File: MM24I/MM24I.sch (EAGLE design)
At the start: 7 parts

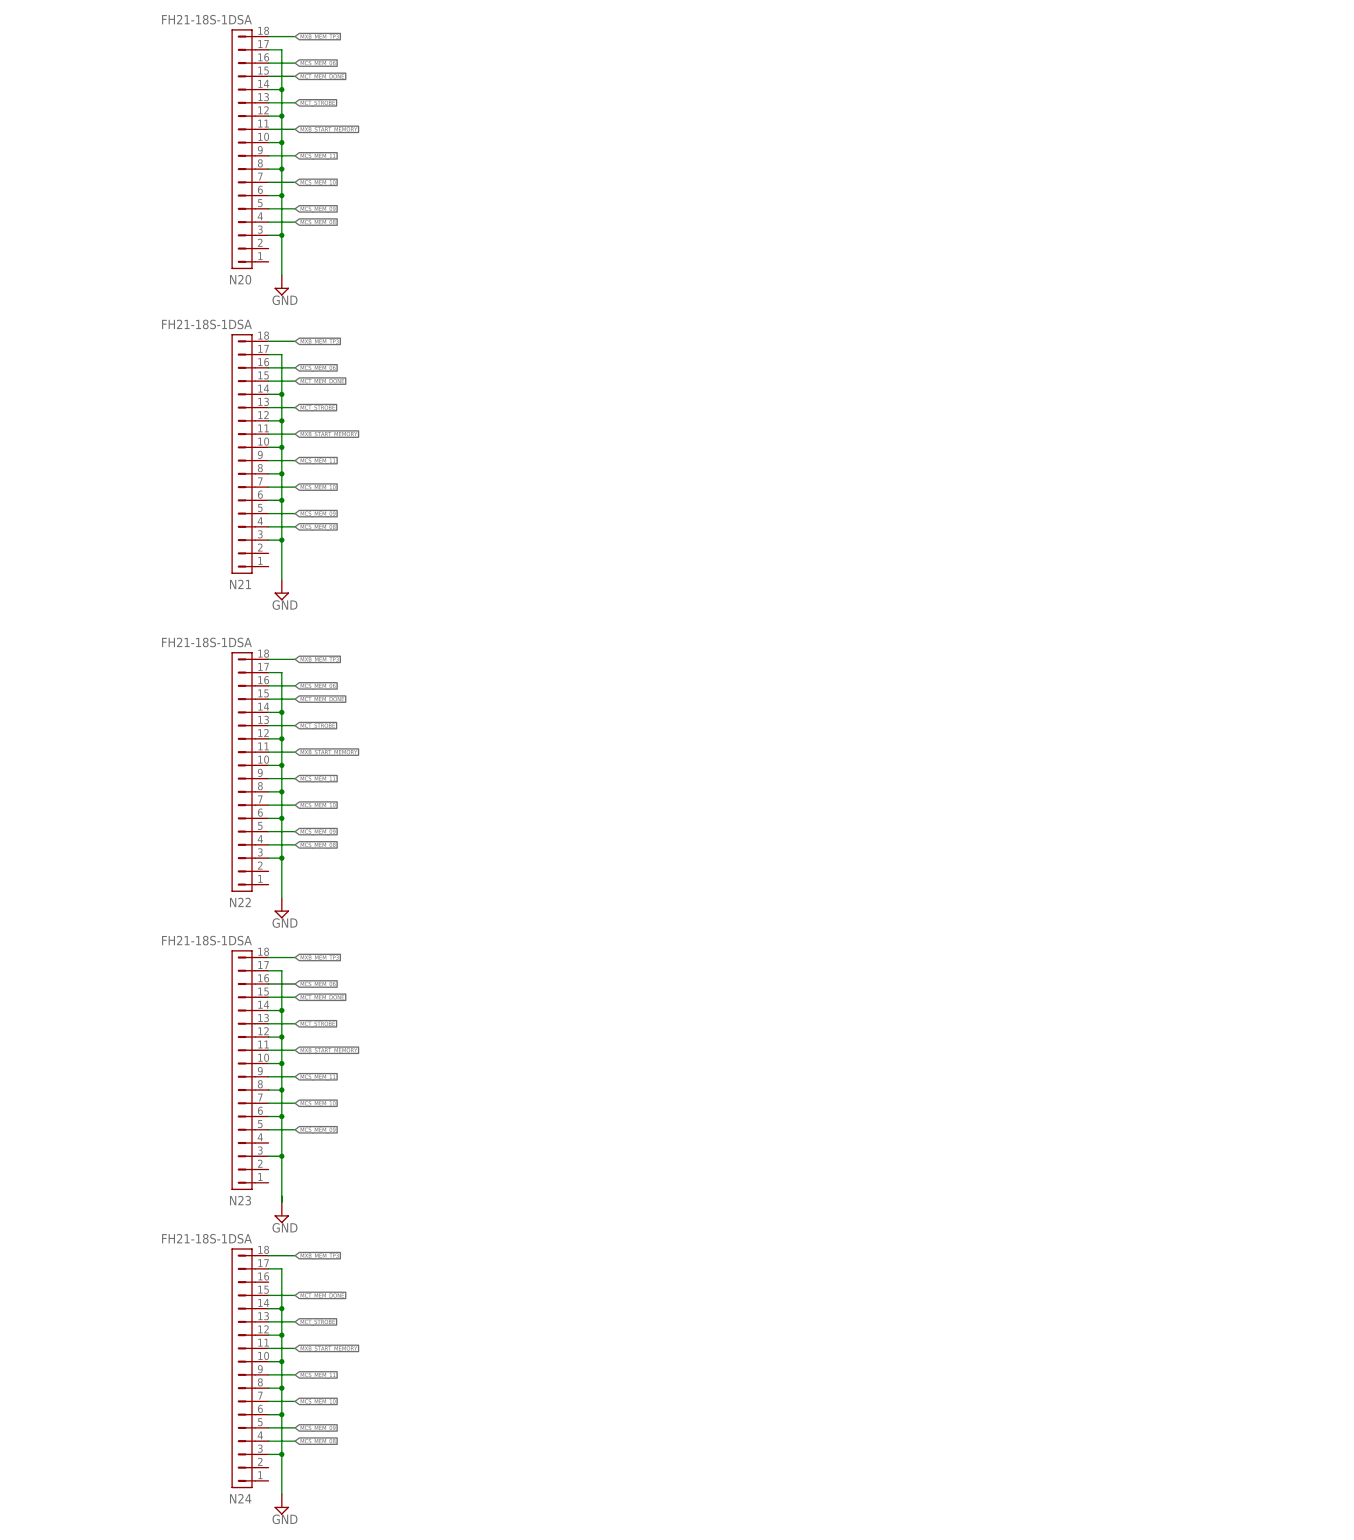
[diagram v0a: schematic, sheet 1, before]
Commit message: Add SN74LVC16T245 16-bit Bus Transceiver/Level Shifter
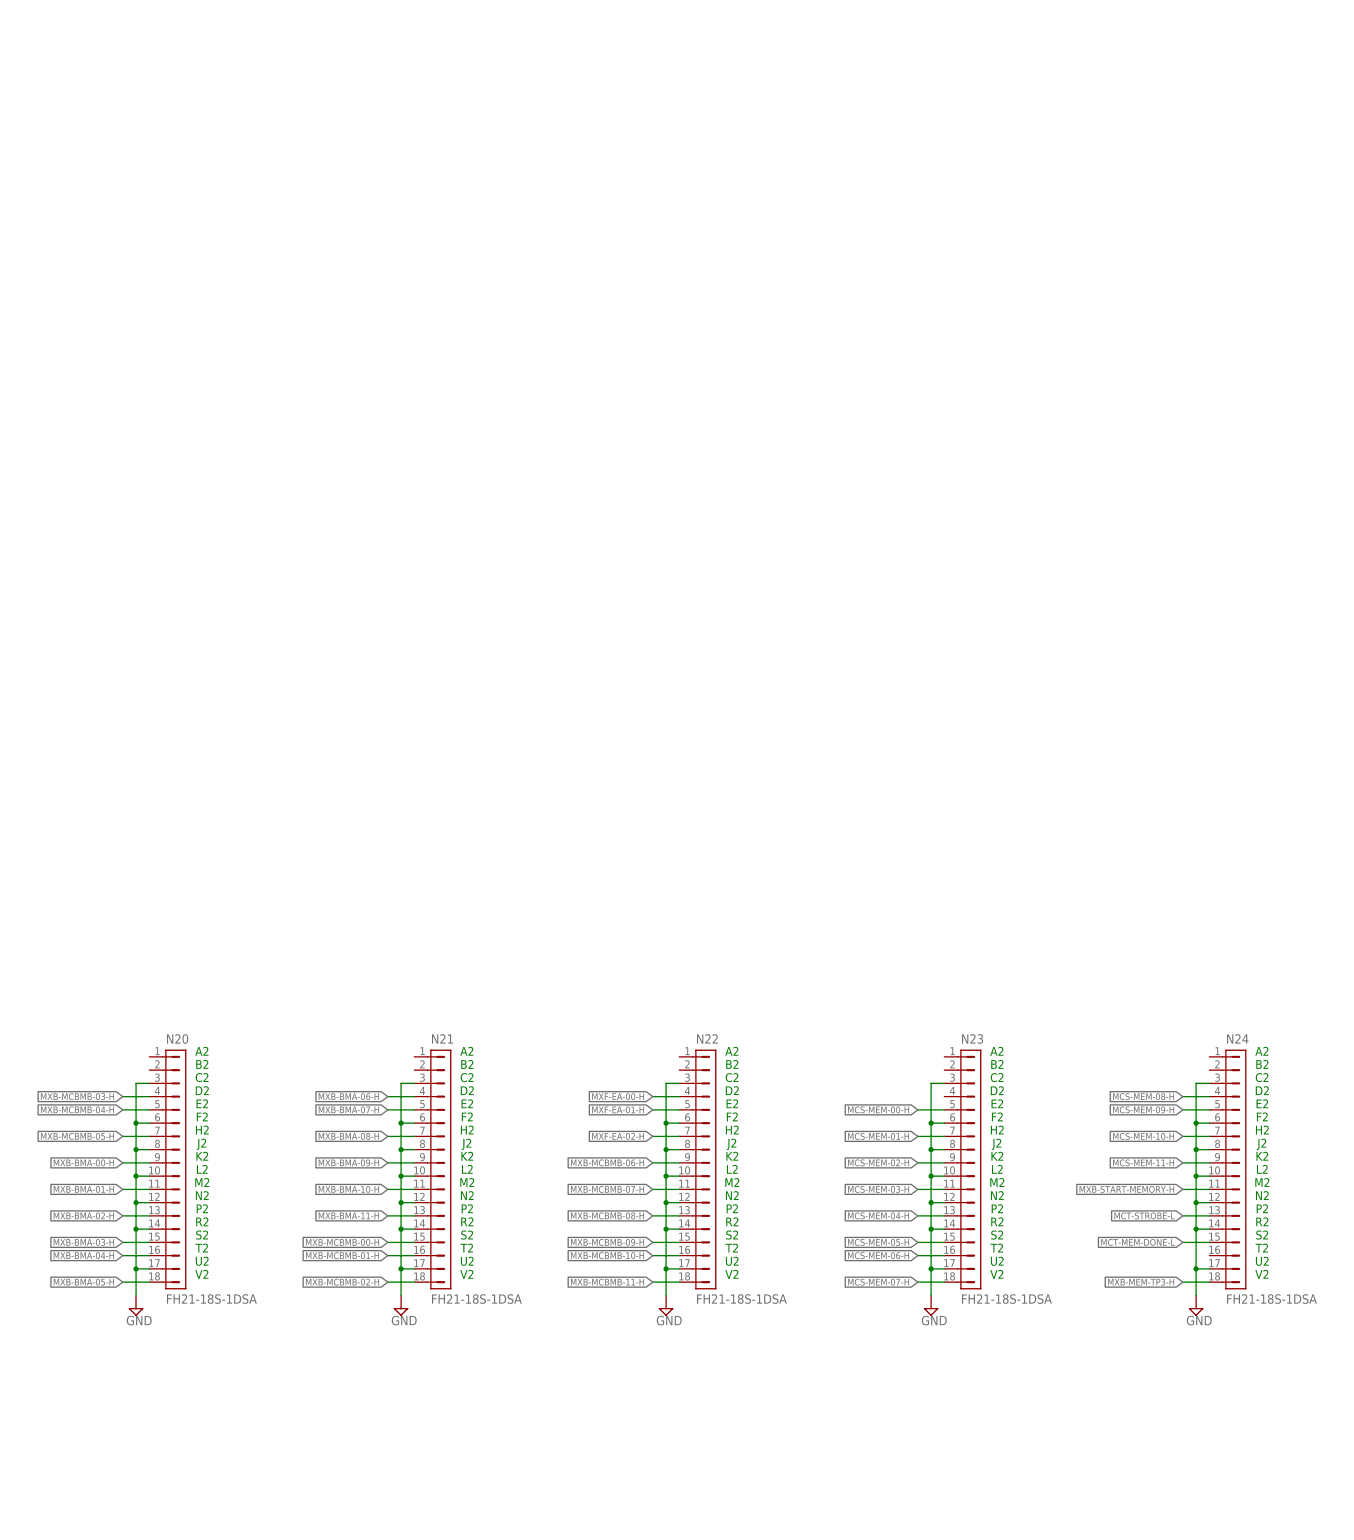
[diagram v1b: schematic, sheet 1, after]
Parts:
- added C2, C3: (no value), rcl:C-USC0805
- added R1, R2, R3, R4: 10k, rcl:R-US_R1206
- added U2: SN74LVC16T245DGVR, MM24I:SN74LVC16T245DGVR
- U1: value (none) -> CY14B104M; device Cypress Memory:CY14B104M -> MM24I:CY14B104M
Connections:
- removed net MCS_MEM_06: N20.16, N21.16, N22.16, N23.16
- removed net MCS_MEM_08: N20.4, N21.4, N22.4, N24.4
- removed net MCS_MEM_09: N20.5, N21.5, N22.5, N23.5, N24.5
- removed net MCS_MEM_10: N20.7, N21.7, N22.7, N23.7, N24.7
- removed net MCS_MEM_11: N20.9, N21.9, N22.9, N23.9, N24.9
- removed net MCT_MEM_DONE: N20.15, N21.15, N22.15, N23.15, N24.15
- removed net MCT_STROBE: N20.13, N21.13, N22.13, N23.13, N24.13
- removed net MXB_MEM_TP3: N20.18, N21.18, N22.18, N23.18, N24.18
- removed net MXB_START_MEMORY: N20.11, N21.11, N22.11, N23.11, N24.11
- new net !WE: U1.!WE, U2.1DIR, U2.2DIR
- new net +5V: C3.2
- new net MCS-MEM-00-H: N23.5
- new net MCS-MEM-01-H: N23.7
- new net MCS-MEM-02-H: N23.9
- new net MCS-MEM-03-H: N23.11
- new net MCS-MEM-04-H: N23.13
- new net MCS-MEM-05-H: N23.15
- new net MCS-MEM-06-H: N23.16
- new net MCS-MEM-07-H: N23.18
- new net MCS-MEM-08-H: N24.4
- new net MCS-MEM-09-H: N24.5
- new net MCS-MEM-10-H: N24.7
- new net MCS-MEM-11-H: N24.9
- new net MCT-MEM-DONE-L: N24.15
- new net MCT-STROBE-L: N24.13
- new net MXB-BMA-00-H: N20.9
- new net MXB-BMA-01-H: N20.11
- new net MXB-BMA-02-H: N20.13
- new net MXB-BMA-03-H: N20.15
- new net MXB-BMA-04-H: N20.16
- new net MXB-BMA-05-H: N20.18
- new net MXB-BMA-06-H: N21.4
- new net MXB-BMA-07-H: N21.5
- new net MXB-BMA-08-H: N21.7
- new net MXB-BMA-09-H: N21.9
- new net MXB-BMA-10-H: N21.11
- new net MXB-BMA-11-H: N21.13
- new net MXB-MCBMB-00-H: N21.15
- new net MXB-MCBMB-01-H: N21.16
- new net MXB-MCBMB-02-H: N21.18
- new net MXB-MCBMB-03-H: N20.4
- new net MXB-MCBMB-04-H: N20.5
- new net MXB-MCBMB-05-H: N20.7
- new net MXB-MCBMB-06-H: N22.9
- new net MXB-MCBMB-07-H: N22.11
- new net MXB-MCBMB-08-H: N22.13
- new net MXB-MCBMB-09-H: N22.15
- new net MXB-MCBMB-10-H: N22.16
- new net MXB-MCBMB-11-H: N22.18
- new net MXB-MEM-TP3-H: N24.18
- new net MXB-START-MEMORY-H: N24.11
- new net MXF-EA-00-H: N22.4
- new net MXF-EA-01-H: N22.5
- new net MXF-EA-02-H: N22.7
- new net N$10: R4.1, U1.DQ15
- new net N$11: U1.DQ6, U2.1A7
- new net N$12: R1.1, U1.DQ12
- new net N$13: U1.DQ7, U2.1A8
- new net N$14: U1.DQ8, U2.2A1
- new net N$15: U1.DQ9, U2.2A2
- new net N$16: U1.DQ10, U2.2A3
- new net N$17: U1.DQ11, U2.2A4
- new net N$18: U2.1B1
- new net N$19: U2.1B2
- new net N$20: U2.1B3
- new net N$21: U2.1B4
- new net N$22: U2.1B5
- new net N$23: U2.1B6
- new net N$24: U2.1B7
- new net N$25: U2.1B8
- new net N$26: U2.2B1
- new net N$27: U2.2B2
- new net N$28: U2.2B3
- new net N$29: U2.2B4
- new net N$3: U1.DQ1, U2.1A2
- new net N$30: C3.1, U2.VCCB, U2.VCCB_2
- new net N$31: C2.1, U2.VCCA, U2.VCCA_2
- new net N$4: U1.DQ2, U2.1A3
- new net N$5: U1.DQ3, U2.1A4
- new net N$6: U1.DQ4, U2.1A5
- new net N$7: U1.DQ5, U2.1A6
- new net N$8: R2.1, U1.DQ13
- new net N$9: R3.1, U1.DQ14
- net GND: now also R1.2, R2.2, R3.2, R4.2, U2.!1OE, U2.!2OE, U2.2A5, U2.2A6, U2.2A7, U2.2A8, U2.2B5, U2.2B6, U2.2B7, U2.2B8, U2.GND, U2.GND_2, U2.GND_3, U2.GND_4, U2.GND_5, U2.GND_6, U2.GND_7, U2.GND_8
- net N$2: now also U1.DQ0, U2.1A1; no longer U1.A13, U1.A14, U1.A15, U1.A16, U1.A17
- net VCC: now also C2.2
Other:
- note added: "A2 B2 C2 D2 E2 F2 H2 J2 K2 L2 M2 N2 P2 R2 S2 T2 U2 V2"
- note added: "DIR high = A in to B out (read) DIR low = B in to A out (write)"
- moved on the sheet: C1, N20, N21, N22, N23, N24
